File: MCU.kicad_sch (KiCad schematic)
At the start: 1 part, among them U1 STM32L476RCTx

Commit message: This should be the most recent one
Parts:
- added C3, C4: 100uF, symbol Device:C_US
- added R3, R4: 22Ω, symbol Device:R_US
- added U3: LD1117S33TR, LD1117S33TR:SOT230P700X180-4N, symbol LD1117S33TR:LD1117S33TR
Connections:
- net GND: now reaches U1.12 (VSSA)
- net GND: now also U1.18 (VSS), U1.31 (VSS), U1.47 (VSS), U1.63 (VSS), C3.2, C4.2, U3.1 (GND)
- net at U1.44 (PA11): now also R3.1
- net at U1.45 (PA12): now also R4.1
- new net +3.3V: C4.1, U3.2 (OUT), U3.4 (OUT__1)
- new net +5V: C3.1, U3.3 (IN)
- new net DATA+: R4.2
- new net DATA-: R3.2
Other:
- moved on the sheet: U1

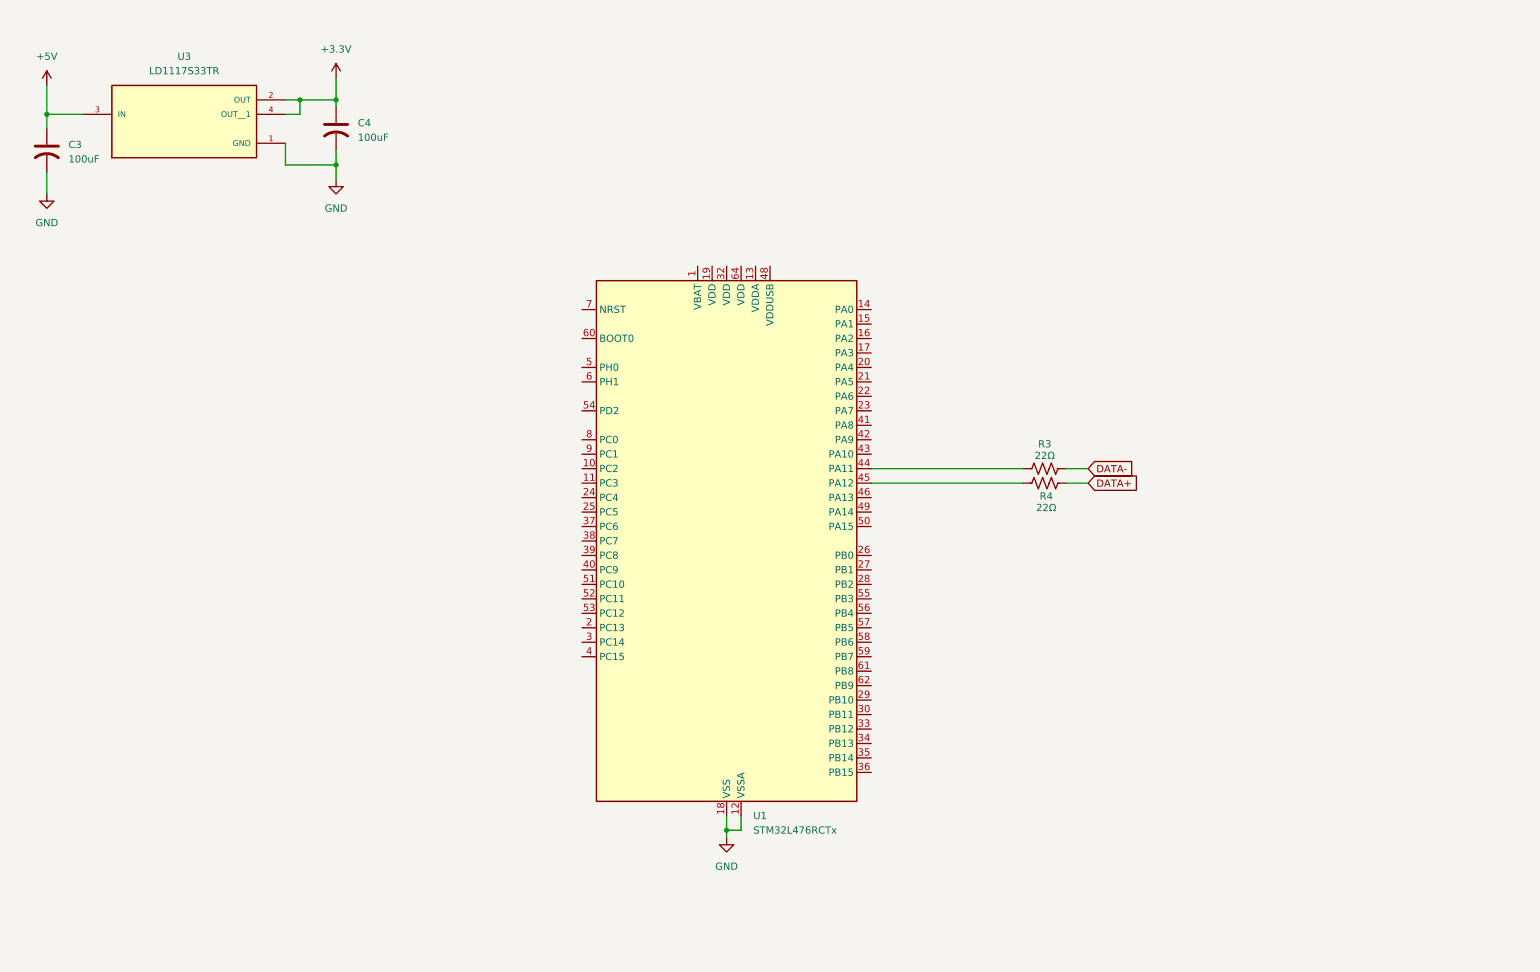
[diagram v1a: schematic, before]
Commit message: Added coupling capacitors for power filtering
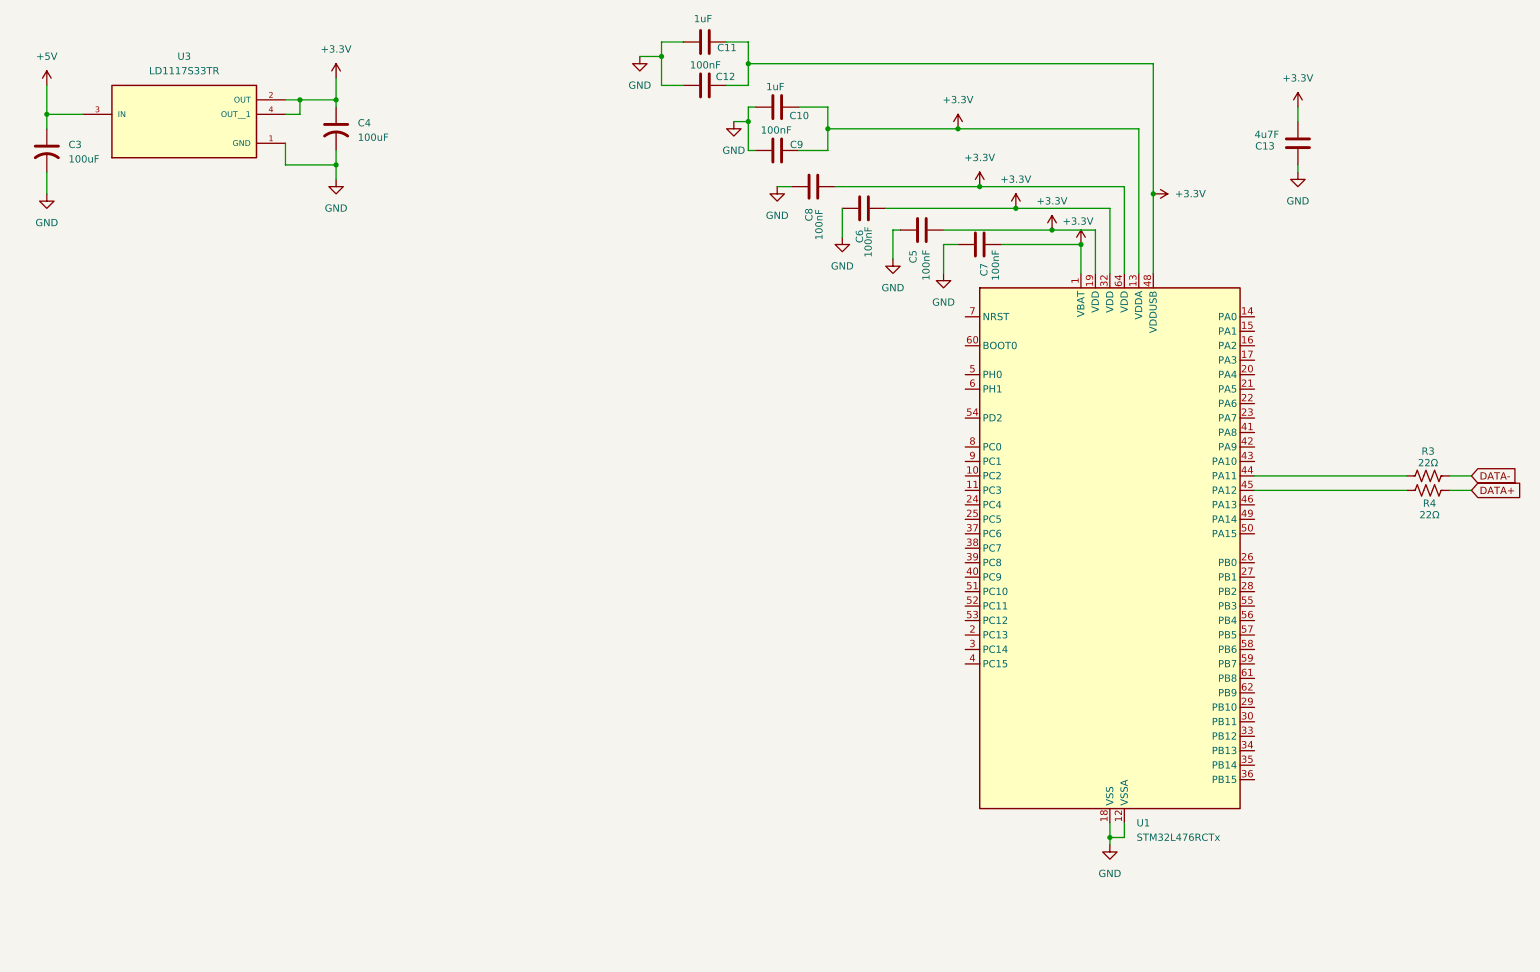
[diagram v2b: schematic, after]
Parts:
- added C10, C11: 1uF, symbol Device:C
- added C12, C5, C6, C7, C8, C9: 100nF, symbol Device:C
- added C13: 4u7F, symbol Device:C
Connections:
- net +3.3V: now also U1.1 (VBAT), U1.13 (VDDA), U1.19 (VDD), U1.32 (VDD), U1.48 (VDDUSB), U1.64 (VDD), C10.2, C11.2, C12.2, C13.2, C5.2, C6.2, C7.2, C8.2, C9.2
- net GND: now also C10.1, C11.1, C12.1, C13.1, C5.1, C6.1, C7.1, C8.1, C9.1
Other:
- moved on the sheet: R3, R4, U1

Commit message: added power switch and RF module
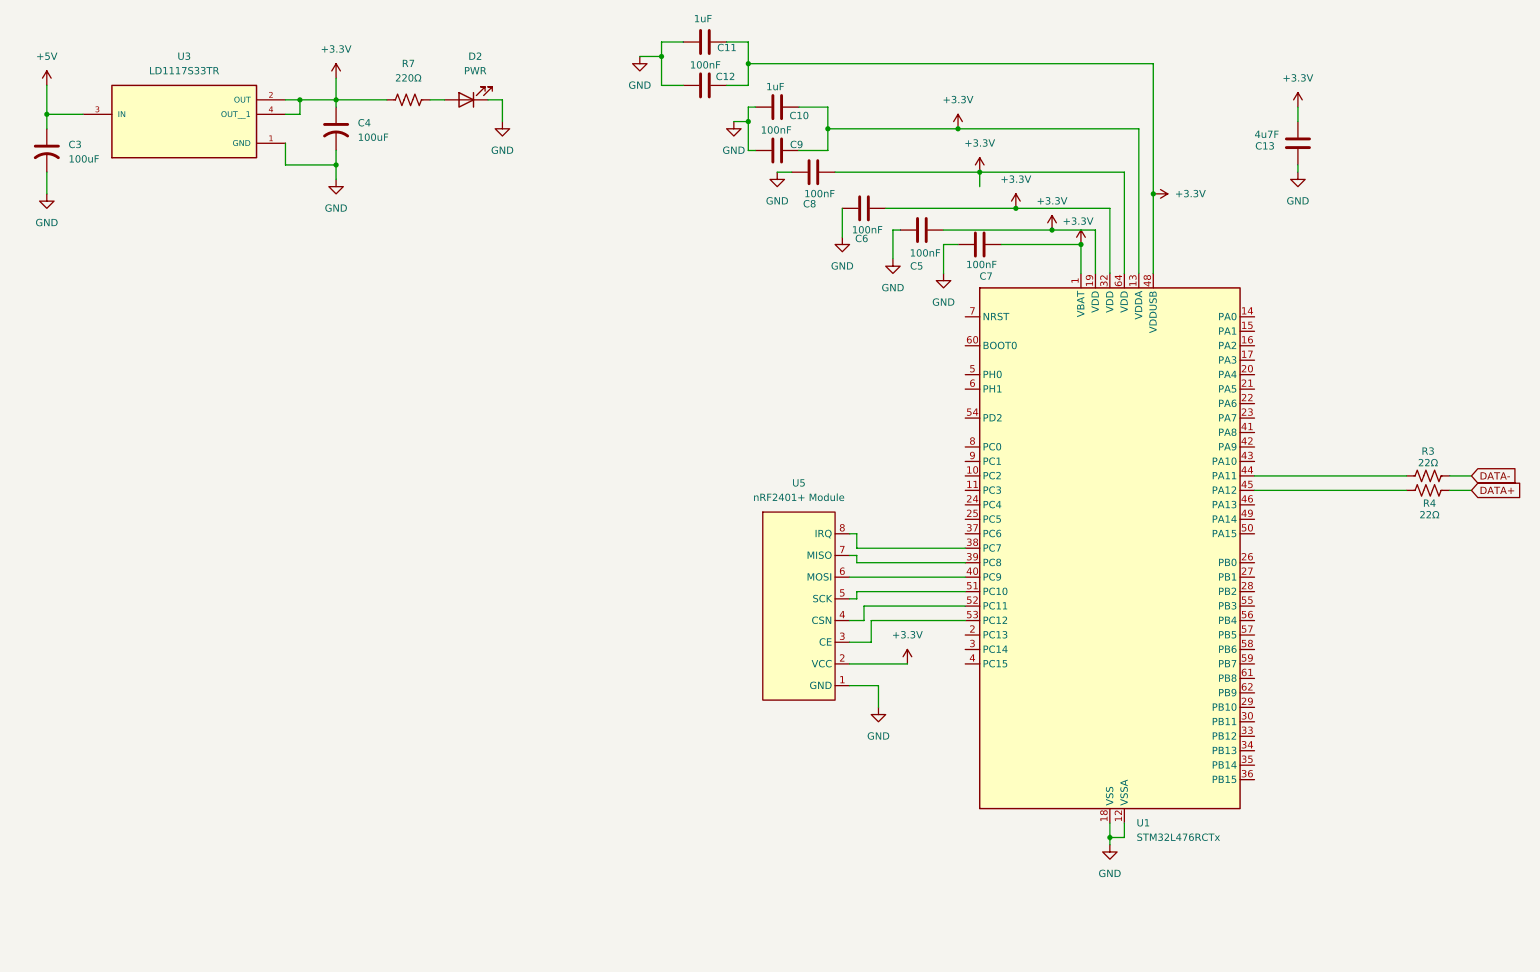
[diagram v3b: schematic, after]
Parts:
- added D2: PWR, symbol Device:LED
- added R7: 220Ω, symbol Device:R_US
- added U5: nRF2401+ Module, symbol nRF2401+_module_board:nRF2401-moduleBoard_1
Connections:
- net +3.3V: now also R7.1, U5.2 (VCC)
- net GND: now also D2.1 (K), U5.1 (GND)
- net at U1.38 (PC7): now also U5.8 (IRQ)
- net at U1.39 (PC8): now also U5.7 (MISO)
- net at U1.40 (PC9): now also U5.6 (MOSI)
- net at U1.51 (PC10): now also U5.5 (SCK)
- net at U1.52 (PC11): now also U5.4 (CSN)
- net at U1.53 (PC12): now also U5.3 (CE)
- new net: D2.2 (A), R7.2
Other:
- moved on the sheet: C8

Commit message: Everything is done except for the programming pins
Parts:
- added C19, C20: 8pF, symbol Device:C_Small_US
- added LED1: LTST-C171KRKT, LED_LTST-C171_LTO, symbol LTST-C171KRKT(red-LED):LTST-C171KRKT
- added LS1: AI-1223-TWT-3V-2-R, AI-1223-TWT-3V-2-R:XDCR_AI-1223-TWT-3V-2-R, symbol AI-1223-TWT-3V-2-R:AI-1223-TWT-3V-2-R
- added R10: 330Ω, symbol Device:R_US
- added R15: 1kΩ, symbol Device:R_US
- added R16: R_EXT, symbol Device:R_Small_US
- added SW1: D6R90F2LFS, D6R90_CNK, symbol D6R90_F2(push-button):D6R90F2LFS
- added X1: CG04874-8M, XTAL_CG04874_NDK, symbol CG04847-8M-XTAL:CG04874-8M
- C10, C11, C12, C5, C6, C7, C8, C9: symbol Device:C -> Device:C_US
- R7: value 220Ω -> 330Ω
- U5: footprint (none) -> nRF2401+_moduleBoard:HiLetgo-nRF2041+module
- renumbered D2 to LED1
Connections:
- net GND: now also C19.2, C20.2, LED1.1, LS1.N, SW1.2
- net at U1.2 (PC13): now also U5.5 (SCK)
- net BUZZ: now reaches U1.26 (PB0)
- net BUZZ: now also R15.2
- net RLED: now reaches U1.27 (PB1)
- net RLED: now also R10.1
- net PUSH: now reaches U1.28 (PB2)
- net PUSH: now also SW1.1
- net LCD_E: now reaches U1.29 (PB10)
- net at U1.3 (PC14): now also U5.4 (CSN)
- net LCD_SR: now reaches U1.30 (PB11)
- net LCD4: now reaches U1.33 (PB12)
- net LCD5: now reaches U1.34 (PB13)
- net LCD6: now reaches U1.35 (PB14)
- net LCD7: now reaches U1.36 (PB15)
- net at U1.38 (PC7): no longer U5.8 (IRQ)
- net at U1.39 (PC8): no longer U5.7 (MISO)
- net at U1.4 (PC15): now also U5.3 (CE)
- net at U1.40 (PC9): no longer U5.6 (MOSI)
- net at U1.5 (PH0): now also C20.1, X1.1
- net at U1.51 (PC10): now also U5.8 (IRQ); no longer U5.5 (SCK)
- net at U1.52 (PC11): now also U5.7 (MISO); no longer U5.4 (CSN)
- net at U1.53 (PC12): now also U5.6 (MOSI); no longer U5.3 (CE)
- net at U1.6 (PH1): now also R16.2
- new net: LS1.P, R15.1
- new net: C19.1, R16.1, X1.2
- new net: LED1.2, R10.2
- no-connect marks 0 -> 2
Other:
- moved on the sheet: C10, C11, C12, C13, C3, C4, C5, C6, C7, C8, C9, LED1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

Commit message: Edits
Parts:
- added J3: SWD Reset, Connector_PinHeader_2.54mm:PinHeader_1x05_P2.54mm, symbol Connector_Generic:Conn_01x01
- added J4: SWDIO, Connector_PinHeader_2.54mm:PinHeader_1x05_P2.54mm, symbol Connector_Generic:Conn_01x01
- added J5: SWCLK, Connector_PinHeader_2.54mm:PinHeader_1x05_P2.54mm, symbol Connector_Generic:Conn_01x01
- added J6, J7: Conn_01x01, Connector_PinHeader_2.54mm:PinHeader_1x05_P2.54mm, symbol Connector_Generic:Conn_01x01
- C10: renamed from C5; footprint (none) -> Capacitor_SMD:C_01005_0402Metric
- C11: renamed from C6; footprint (none) -> Capacitor_SMD:C_01005_0402Metric
- C12: renamed from C8; footprint (none) -> Capacitor_SMD:C_01005_0402Metric
- C13: renamed from C10; footprint (none) -> Capacitor_SMD:C_01005_0402Metric
- C14: renamed from C9; footprint (none) -> Capacitor_SMD:C_01005_0402Metric
- C15: renamed from C11; footprint (none) -> Capacitor_SMD:C_01005_0402Metric
- C16: renamed from C12; footprint (none) -> Capacitor_SMD:C_01005_0402Metric
- C17: renamed from C13; footprint (none) -> Capacitor_SMD:C_01005_0402Metric
- C5: renamed from C3; footprint (none) -> Capacitor_SMD:C_01005_0402Metric
- C6: renamed from C4; footprint (none) -> Capacitor_SMD:C_01005_0402Metric
- C7: renamed from C20; footprint (none) -> Capacitor_SMD:C_01005_0402Metric
- C8: renamed from C19; footprint (none) -> Capacitor_SMD:C_01005_0402Metric
- C9: renamed from C7; footprint (none) -> Capacitor_SMD:C_01005_0402Metric
- R10: renamed from R15; footprint (none) -> Resistor_SMD:R_0402_1005Metric
- R11: renamed from R10; footprint (none) -> Resistor_SMD:R_0402_1005Metric
- R6: renamed from R7; footprint (none) -> Resistor_SMD:R_0402_1005Metric
- R7: renamed from R16; footprint (none) -> Resistor_SMD:R_0402_1005Metric
- R8: renamed from R3; footprint (none) -> Resistor_SMD:R_0402_1005Metric
- R9: renamed from R4; footprint (none) -> Resistor_SMD:R_0402_1005Metric
- renumbered LED1 to LED2, LED1 to LED3, LS1 to LS2, SW1 to SW2, U3 to U4, U1 to U6, X1 to X2
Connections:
- net +3.3V: now also J6.1 (Pin_1)
- net GND: now also J7.1 (Pin_1)
- net at U6.46 (PA13): now also J4.1 (Pin_1)
- net at U6.49 (PA14): now also J5.1 (Pin_1)
- net at U6.7 (NRST): now also J3.1 (Pin_1)
- no-connect marks 2 -> 33

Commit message: Last edits
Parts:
- J3, J4, J5, J6, J7: footprint Connector_PinHeader_2.54mm:PinHeader_1x05_P2.54mm -> Connector_PinHeader_2.54mm:PinHeader_1x05_P2.54mm_Vertical
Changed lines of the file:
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@@
 	(wire
 		(pts
-			(xy 69.85 21.59) (xy 69.85 25.4)
-		)
-		(stroke
-			(width 0)
-			(type default)
-		)
-	)
-	(wire
-		(pts
 			(xy 200.66 118.11) (xy 190.5 118.11)
 		)
@@
 	(wire
 		(pts
+			(xy 63.5 21.59) (xy 63.5 25.4)
+		)
+		(stroke
+			(width 0)
+			(type default)
+		)
+	)
+	(wire
+		(pts
 			(xy 60.96 27.94) (xy 63.5 27.94)
 		)
@@
 	)
 	(symbol
-		(lib_id "power:+3.3V")
-		(at 69.85 21.59 0)
-		(unit 1)
-		(exclude_from_sim no)
-		(in_bom yes)
-		(on_board yes)
-		(dnp no)
-		(fields_autoplaced yes)
-		(property "Reference" "#PWR020"
-			(at 69.85 25.4 0)
-			(effects
-				(font
-					(size 1.27 1.27)
-				)
-				(hide yes)
-			)
-		)
-		(property "Value" "+3.3V"
-			(at 69.85 16.51 0)
-			(effects
-				(font
-					(size 1.27 1.27)
-				)
-			)
-		)
-		(property "Footprint" ""
-			(at 69.85 21.59 0)
-			(effects
-				(font
-					(size 1.27 1.27)
-				)
-				(hide yes)
-			)
-		)
-		(property "Datasheet" ""
-			(at 69.85 21.59 0)
-			(effects
-				(font
-					(size 1.27 1.27)
-				)
-				(hide yes)
-			)
-		)
-		(property "Description" "Power symbol creates a global label with name \"+3.3V\""
-			(at 69.85 21.59 0)
-			(effects
-				(font
-					(size 1.27 1.27)
-				)
-				(hide yes)
-			)
-		)
-		(pin "1"
-		)
-		(instances
-			(project ""
-				(path "/bcf3418e-986f-42d9-beb5-94c6e2a384e4/4ee1802f-ee07-4d8e-aeda-b2298c2416b2"
-					(reference "#PWR020")
-					(unit 1)
-				)
-			)
-		)
-	)
-	(symbol
 		(lib_id "D6R90_F2(push-button):D6R90F2LFS")
 		(at 245.11 95.25 0)
@@
 			)
 		)
-		(property "Footprint" "Connector_PinHeader_2.54mm:PinHeader_1x05_P2.54mm"
+		(property "Footprint" "Connector_PinHeader_2.54mm:PinHeader_1x05_P2.54mm_Vertical"
 			(at 205.74 133.35 0)
 			(effects
@@
 			)
 		)
-		(property "Footprint" "Connector_PinHeader_2.54mm:PinHeader_1x05_P2.54mm"
+		(property "Footprint" "Connector_PinHeader_2.54mm:PinHeader_1x05_P2.54mm_Vertical"
 			(at 205.74 118.11 0)
 			(effects
@@
 			)
 		)
-		(property "Footprint" "Connector_PinHeader_2.54mm:PinHeader_1x05_P2.54mm"
+		(property "Footprint" "Connector_PinHeader_2.54mm:PinHeader_1x05_P2.54mm_Vertical"
 			(at 115.57 80.01 0)
 			(effects
@@
 	)
 	(symbol
+		(lib_id "power:+3.3V")
+		(at 63.5 21.59 0)
+		(unit 1)
+		(exclude_from_sim no)
+		(in_bom yes)
+		(on_board yes)
+		(dnp no)
+		(fields_autoplaced yes)
+		(property "Reference" "#PWR020"
+			(at 63.5 25.4 0)
+			(effects
+				(font
+					(size 1.27 1.27)
+				)
+				(hide yes)
+			)
+		)
+		(property "Value" "+3.3V"
+			(at 63.5 16.51 0)
+			(effects
+				(font
+					(size 1.27 1.27)
+				)
+			)
+		)
+		(property "Footprint" ""
+			(at 63.5 21.59 0)
+			(effects
+				(font
+					(size 1.27 1.27)
+				)
+				(hide yes)
+			)
+		)
+		(property "Datasheet" ""
+			(at 63.5 21.59 0)
+			(effects
+				(font
+					(size 1.27 1.27)
+				)
+				(hide yes)
+			)
+		)
+		(property "Description" "Power symbol creates a global label with name \"+3.3V\""
+			(at 63.5 21.59 0)
+			(effects
+				(font
+					(size 1.27 1.27)
+				)
+				(hide yes)
+			)
+		)
+		(pin "1"
+		)
+		(instances
+			(project "final_project"
+				(path "/bcf3418e-986f-42d9-beb5-94c6e2a384e4/4ee1802f-ee07-4d8e-aeda-b2298c2416b2"
+					(reference "#PWR020")
+					(unit 1)
+				)
+			)
+		)
+	)
+	(symbol
 		(lib_id "Connector_Generic:Conn_01x01")
 		(at 205.74 123.19 0)
@@
 			)
 		)
-		(property "Footprint" "Connector_PinHeader_2.54mm:PinHeader_1x05_P2.54mm"
+		(property "Footprint" "Connector_PinHeader_2.54mm:PinHeader_1x05_P2.54mm_Vertical"
 			(at 205.74 123.19 0)
 			(effects
@@
 			)
 		)
-		(property "Footprint" "Connector_PinHeader_2.54mm:PinHeader_1x05_P2.54mm"
+		(property "Footprint" "Connector_PinHeader_2.54mm:PinHeader_1x05_P2.54mm_Vertical"
 			(at 205.74 128.27 0)
 			(effects
